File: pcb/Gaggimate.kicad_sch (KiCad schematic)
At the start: 69 parts, among them J1 USB_C_Receptacle, J2 Conn_01x02, J3 Conn_01x03, J4 Conn_01x04, J5 Conn_01x04, J6 Conn_01x10, J7 Conn_01x02, J8 Conn_01x02, K1 Relay_SPDT, K2 Relay_SPDT, K3 Relay_SPDT, Q1 MMBT2222, Q2 MMBT2222, Q3 MMBT2222, SW1 SW_Push, SW2 SW_Push, U1 ESP32-S3-WROOM-1, U2 AMS1117-3.3, U6 MAX31855EASA

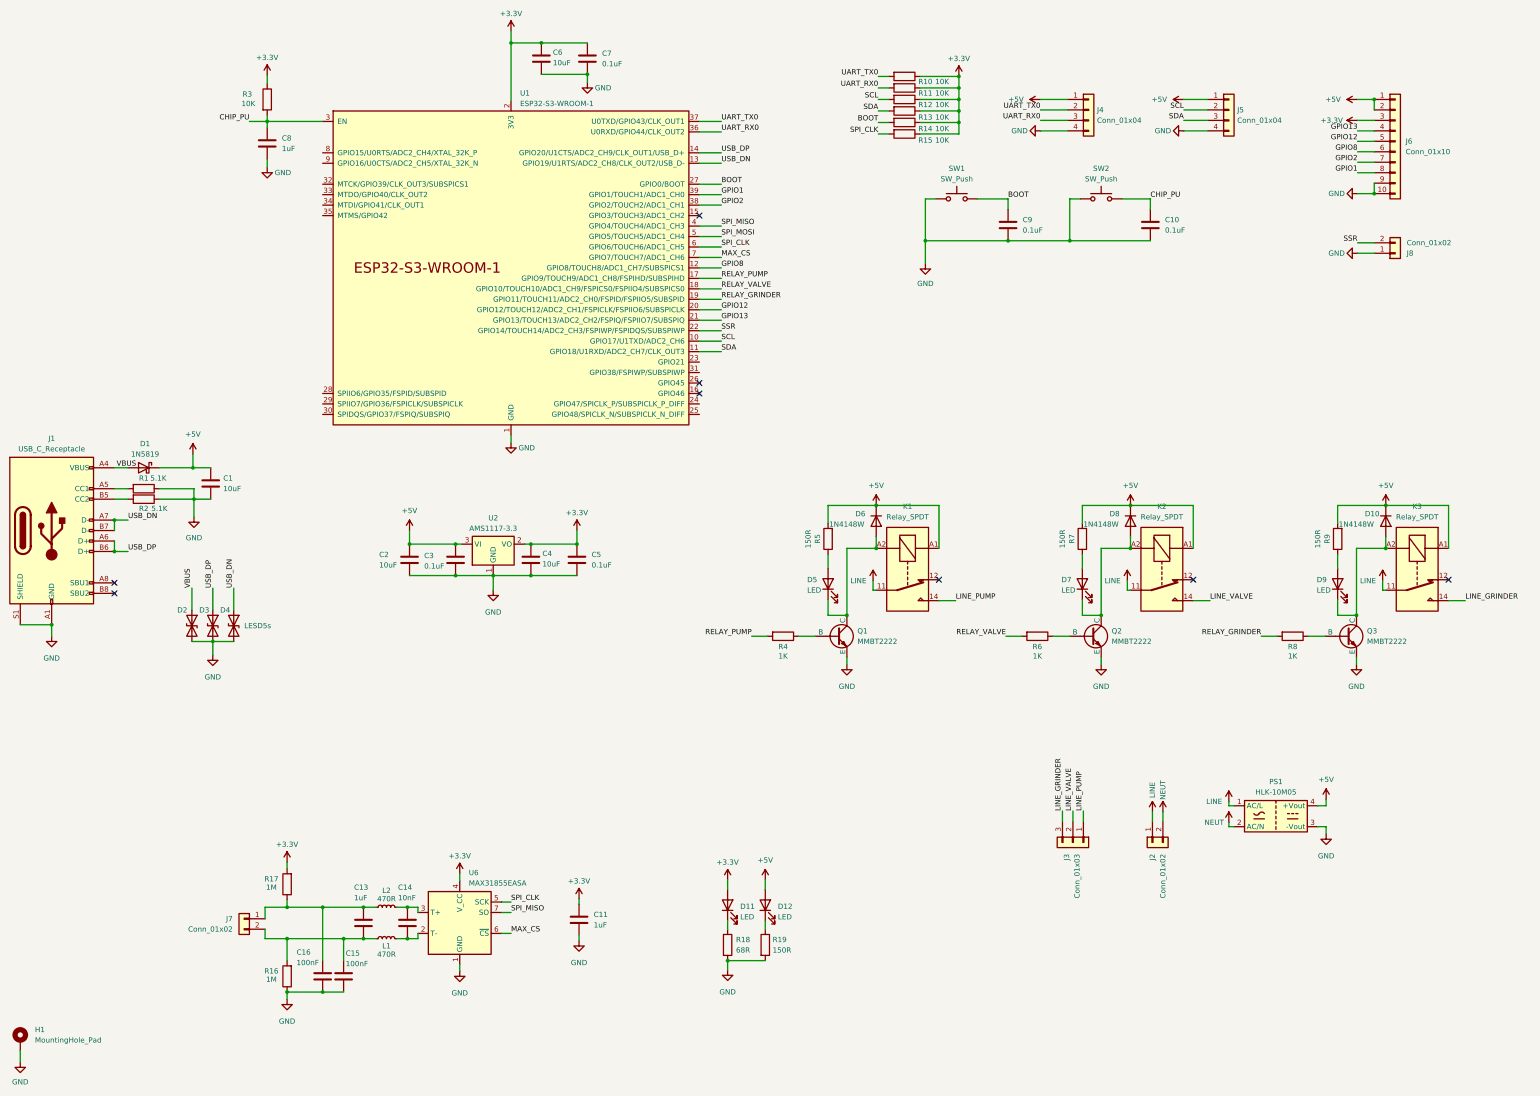
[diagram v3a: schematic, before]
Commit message: feat: Add button connector to PCB, change pcbdraw
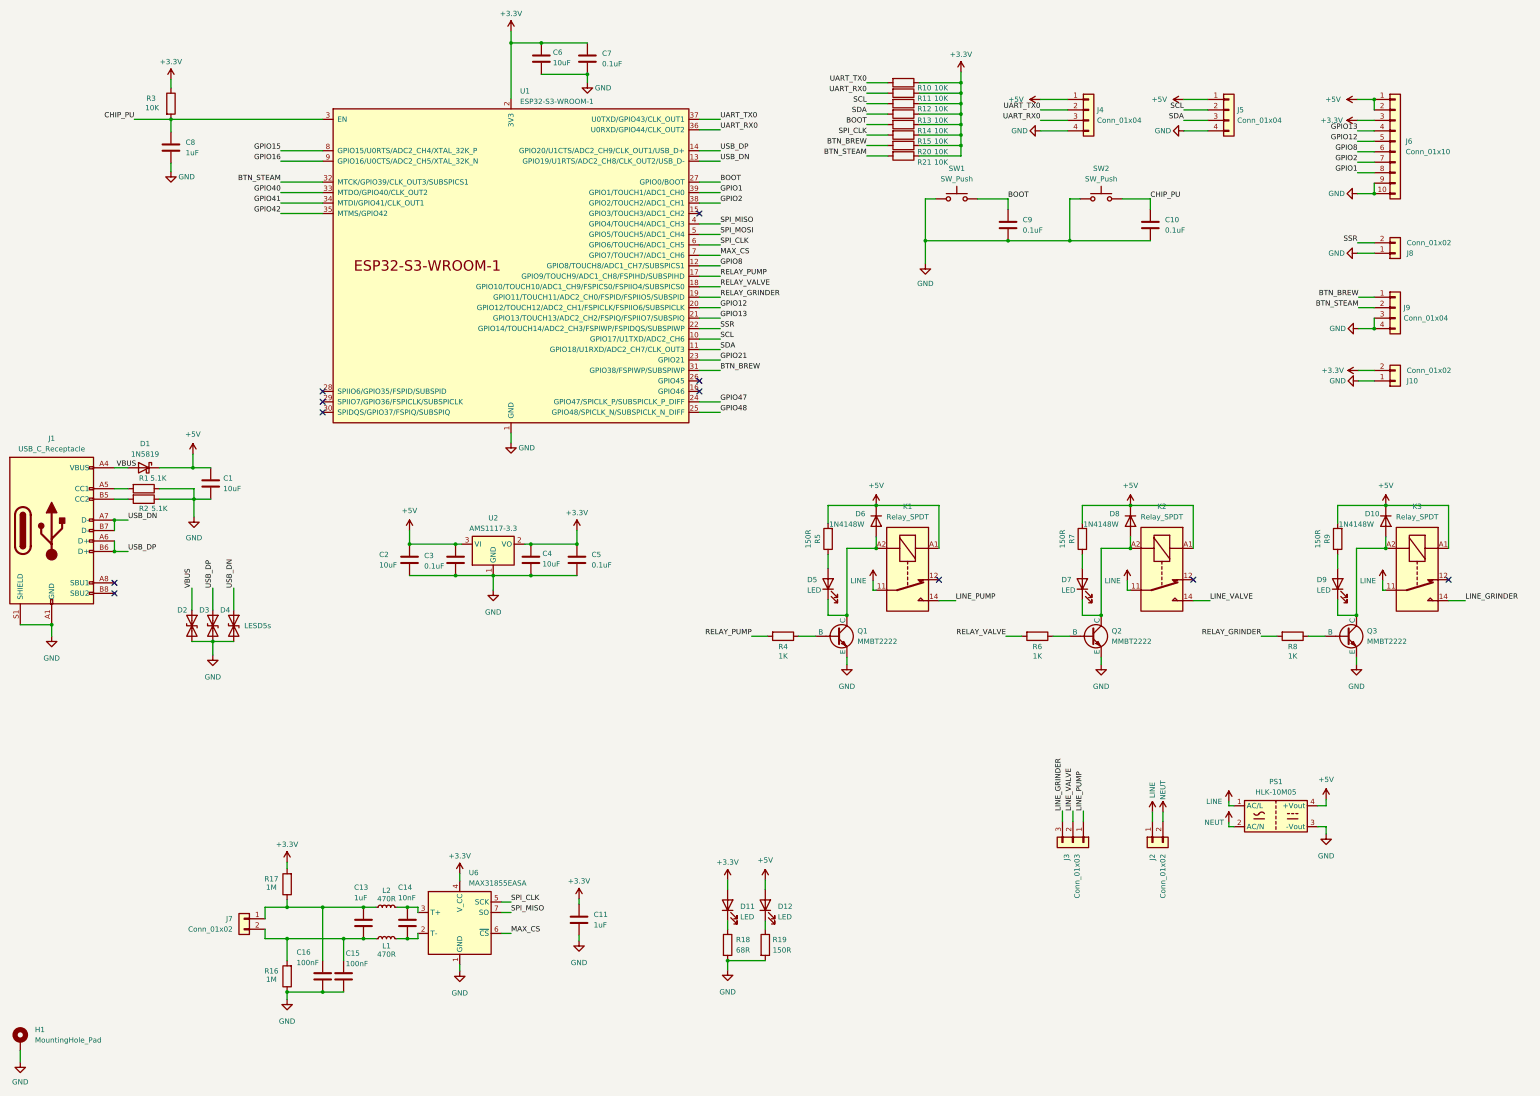
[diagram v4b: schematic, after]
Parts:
- added J10: Conn_01x02, Connector_JST:JST_XH_B2B-XH-A_1x02_P2.50mm_Vertical, symbol Connector_Generic:Conn_01x02
- added J9: Conn_01x04, Connector_JST:JST_XH_B4B-XH-A_1x04_P2.50mm_Vertical, symbol Connector_Generic:Conn_01x04
- added R20, R21: 10K, Resistor_SMD:R_0805_2012Metric, symbol Device:R
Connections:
- net +3.3V: now also J10.2 (Pin_2), R20.1, R21.1
- net GND: now also J10.1 (Pin_1), J9.3 (Pin_3), J9.4 (Pin_4)
- net GPIO21: now reaches U1.23 (GPIO21)
- net GPIO47: now reaches U1.24 (GPIO47/SPICLK_P/SUBSPICLK_P_DIFF)
- net GPIO48: now reaches U1.25 (GPIO48/SPICLK_N/SUBSPICLK_N_DIFF)
- net BTN_BREW: now reaches U1.31 (GPIO38/FSPIWP/SUBSPIWP)
- net BTN_BREW: now also J9.1 (Pin_1), R20.2
- net BTN_STEAM: now reaches U1.32 (MTCK/GPIO39/CLK_OUT3/SUBSPICS1)
- net BTN_STEAM: now also J9.2 (Pin_2), R21.2
- net GPIO40: now reaches U1.33 (MTDO/GPIO40/CLK_OUT2)
- net GPIO41: now reaches U1.34 (MTDI/GPIO41/CLK_OUT1)
- net GPIO42: now reaches U1.35 (MTMS/GPIO42)
- net GPIO15: now reaches U1.8 (GPIO15/U0RTS/ADC2_CH4/XTAL_32K_P)
- net GPIO16: now reaches U1.9 (GPIO16/U0CTS/ADC2_CH5/XTAL_32K_N)
- no-connect marks 8 -> 11
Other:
- moved on the sheet: C8, R10, R11, R12, R13, R14, R3, U1

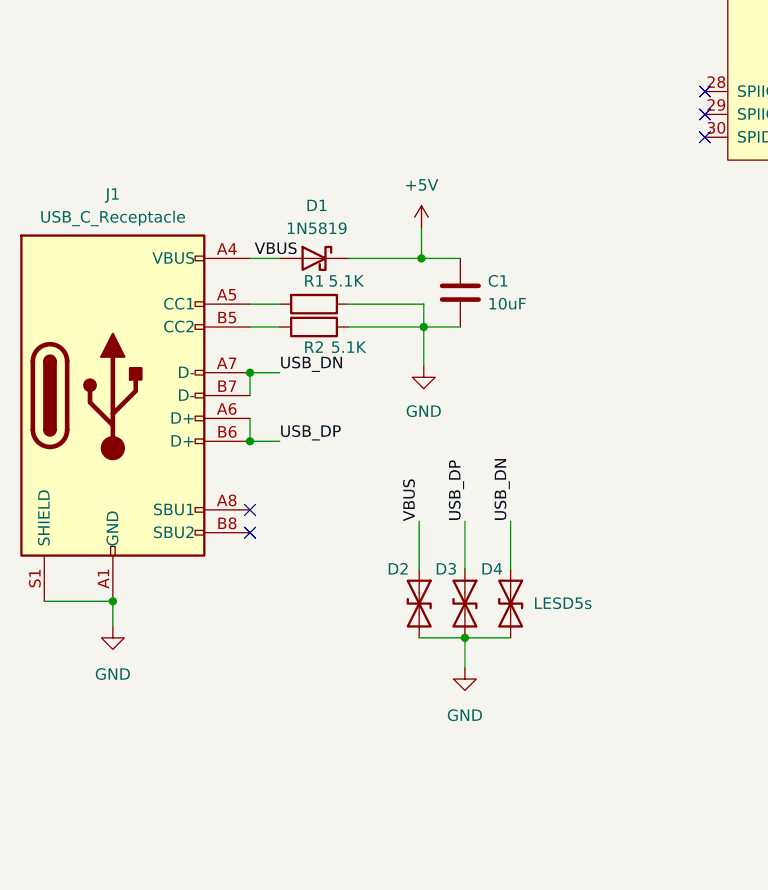
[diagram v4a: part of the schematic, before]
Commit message: feat: Replace diodes with usb protection chip
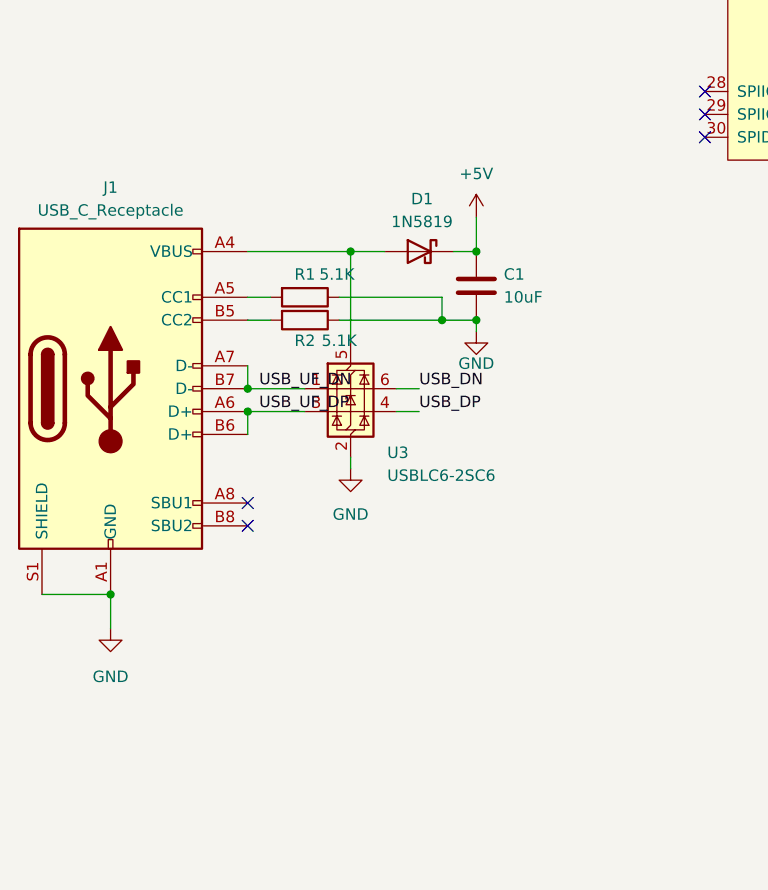
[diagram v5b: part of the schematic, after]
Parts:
- removed D2, D3, D4: LESD5s, Diode_SMD:D_SOD-523, symbol Device:D_TVS
- added U3: USBLC6-2SC6, Package_TO_SOT_SMD:SOT-23-6, symbol Power_Protection:USBLC6-2SC6
- J4, J5: LCSC (none) -> C144395
- J6: LCSC (none) -> C5383117
- J8: LCSC (none) -> C158012
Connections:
- net GND: now also U3.2 (GND)
- net USB_DN: now also U3.6 (I/O1); no longer J1.A7 (D-), J1.B7 (D-)
- net USB_DP: now also U3.4 (I/O2); no longer J1.A6 (D+), J1.B6 (D+)
- net VBUS: no longer names the net of D1.2 (A), J1.A4 (VBUS), J1.A9 (VBUS), J1.B4 (VBUS), J1.B9 (VBUS)
- net VBUS: now also U3.5 (VBUS)
- new net USB_UF_DN: J1.A7 (D-), J1.B7 (D-), U3.1 (I/O1)
- new net USB_UF_DP: J1.A6 (D+), J1.B6 (D+), U3.3 (I/O2)
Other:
- moved on the sheet: C1, D1, J1, R1, R2

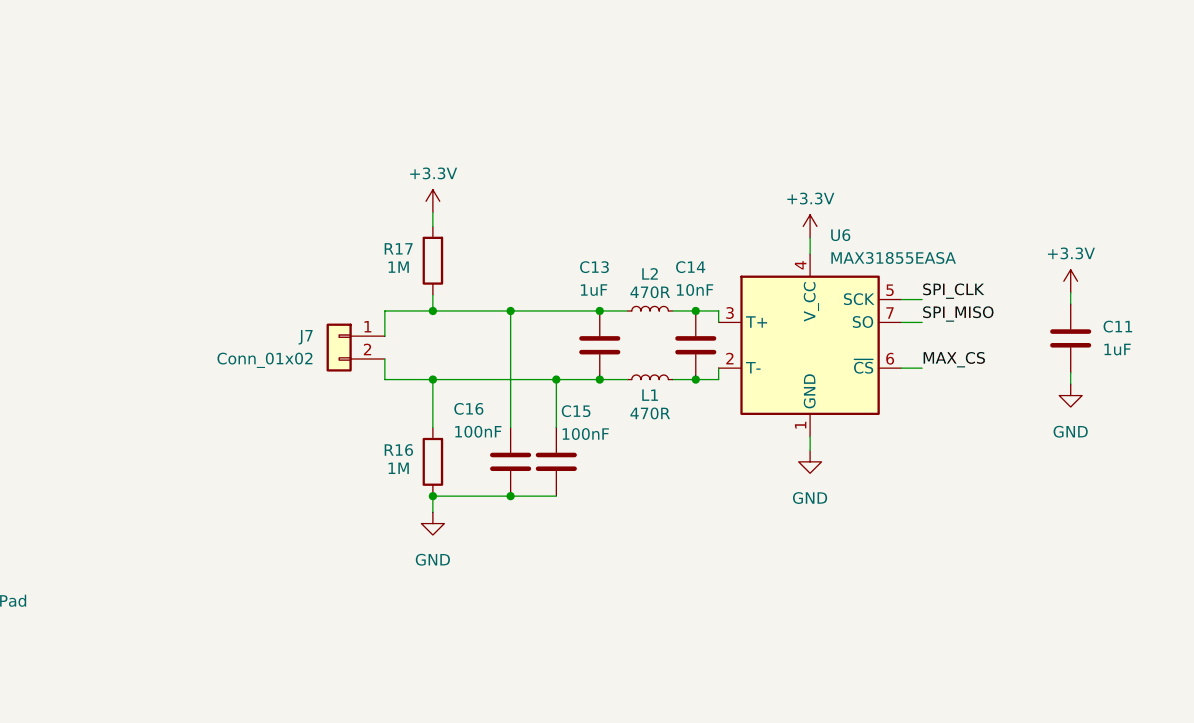
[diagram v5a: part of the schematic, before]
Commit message: feat: Simplify MAX31885 circuit, add silkscreen pinout
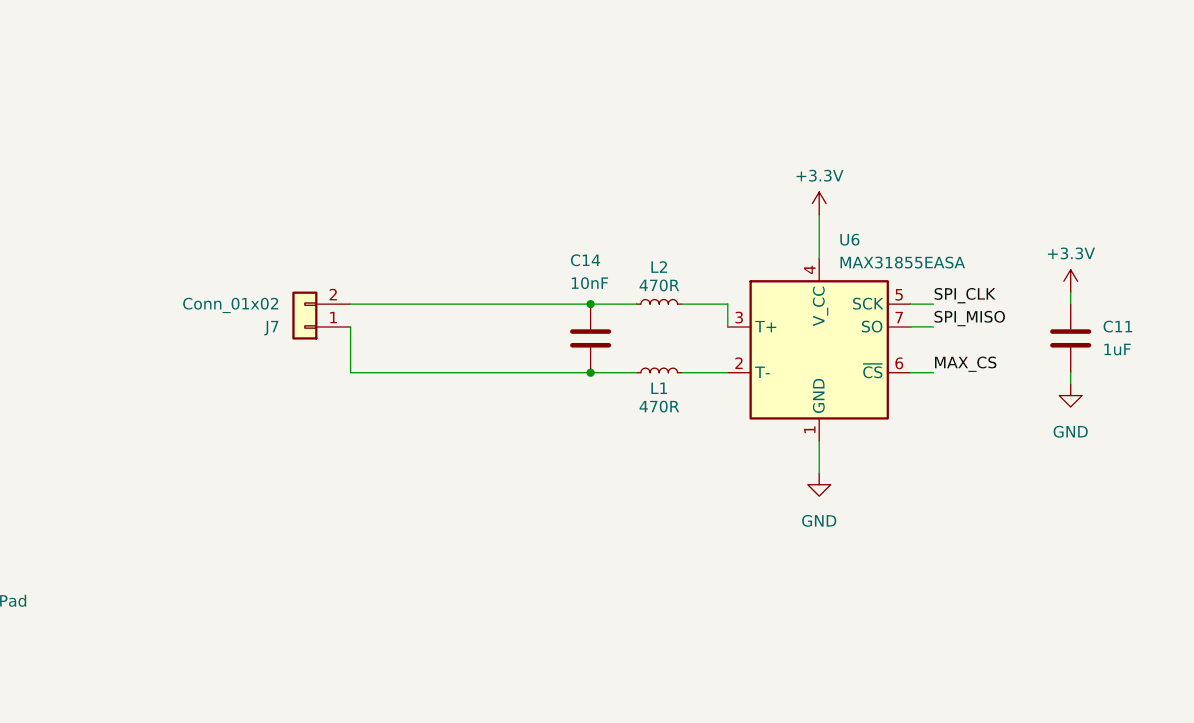
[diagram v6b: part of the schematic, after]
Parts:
- removed C13: 1uF, Capacitor_SMD:C_0805_2012Metric, symbol Device:C
- removed C15, C16: 100nF, Capacitor_SMD:C_0805_2012Metric, symbol Device:C
- removed R16, R17: 1M, Resistor_SMD:R_0805_2012Metric, symbol Device:R
- J10: LCSC (none) -> C158012
- J2: LCSC C2683165 -> C409161
- J3: LCSC C2683166 -> C409163
- J7: LCSC C5481312 -> C415432
- SW1, SW2: LCSC C221896 -> C2909692
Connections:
- net at L1.1: now also C14.2, J7.1 (Pin_1); no longer J7.2 (Pin_2)
- net at L1.2, U6.2 (T-): no longer C14.2
- net at L2.2, U6.3 (T+): no longer C14.1
- net at L2.1: now also C14.1, J7.2 (Pin_2); no longer J7.1 (Pin_1)
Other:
- moved on the sheet: C14, J7, L1, L2, U6

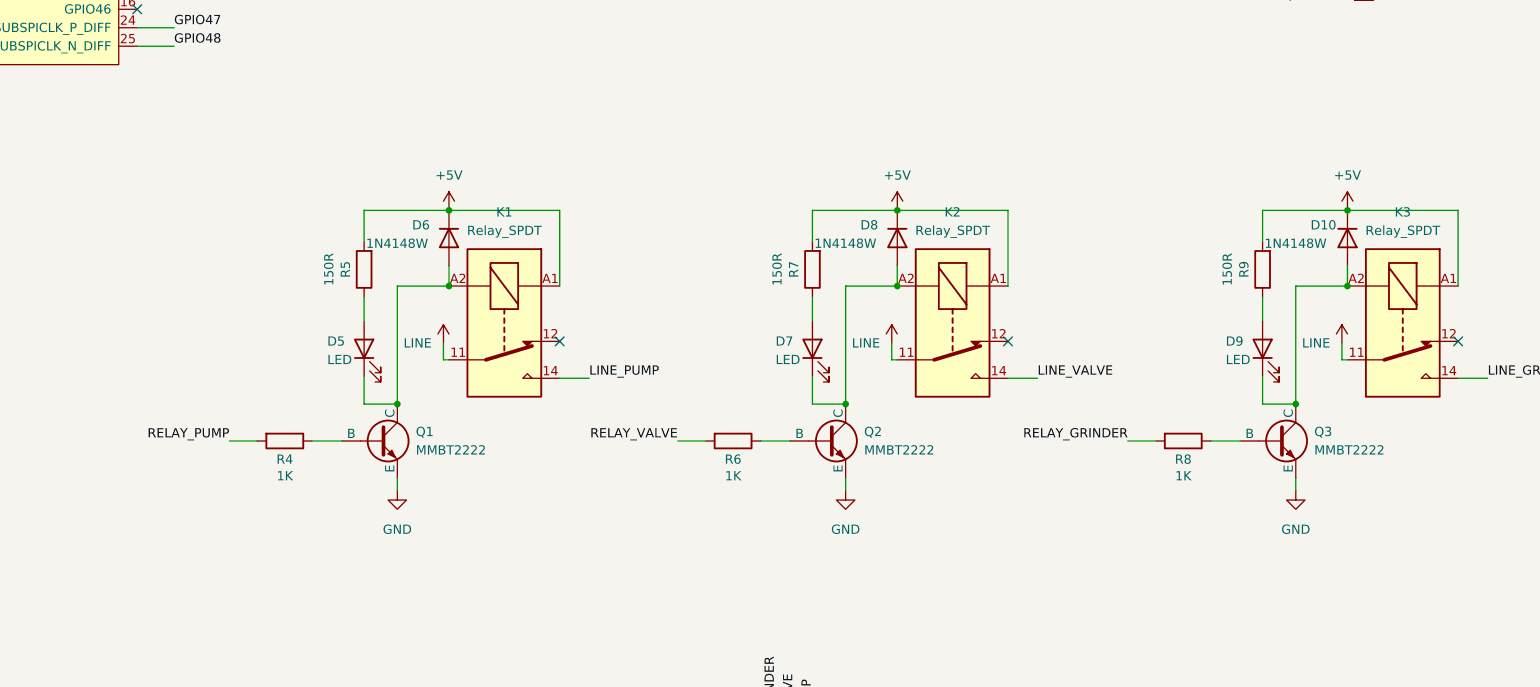
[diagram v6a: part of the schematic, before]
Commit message: feat: Fix PCB label, add render
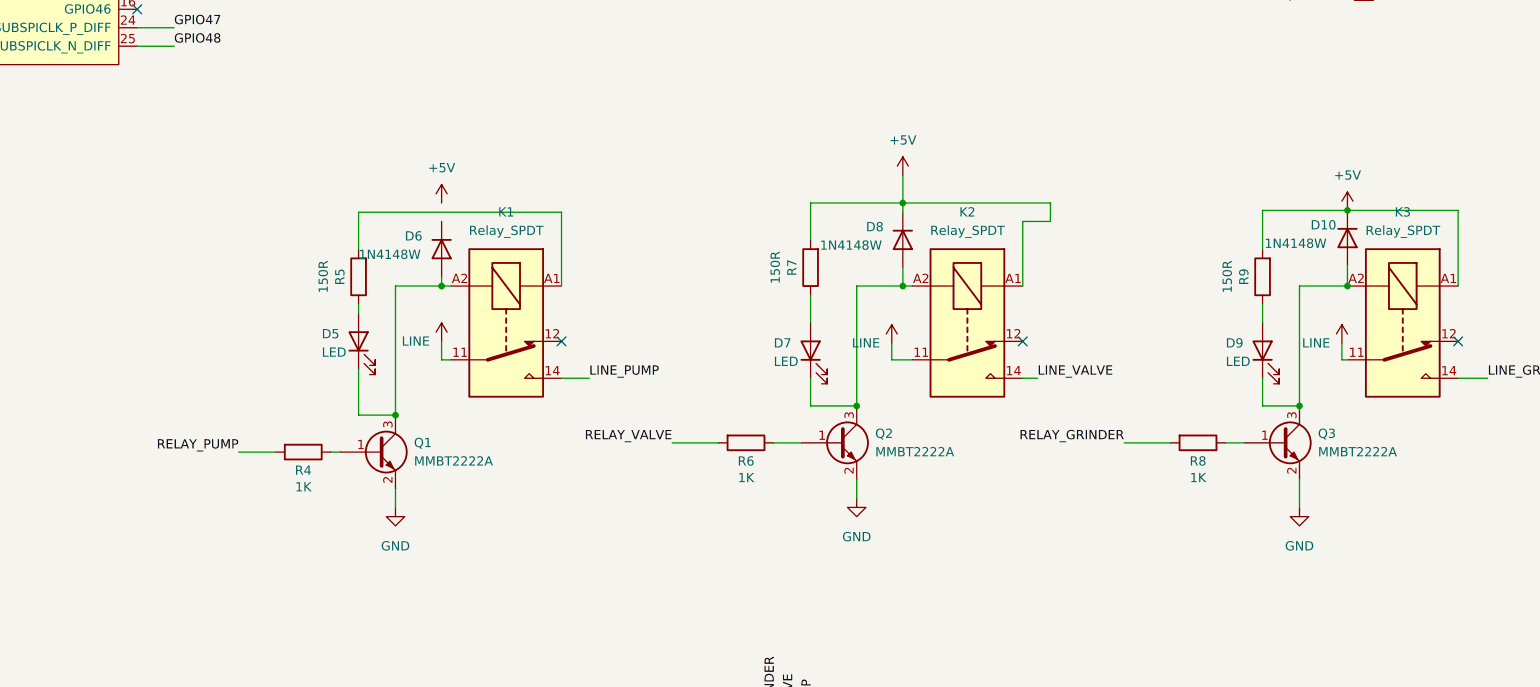
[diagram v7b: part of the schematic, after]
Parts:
- removed Q1, Q2, Q3: MMBT2222, Package_TO_SOT_SMD:SOT-23-3, symbol Simulation_SPICE:NPN
- added Q1, Q2, Q3: MMBT2222A, Package_TO_SOT_SMD:SOT-23, symbol Transistor_BJT:MMBT2222A
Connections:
- net +5V: no longer D6.1 (K), K1.A1, R5.2
- net GND: now also Q1.2 (E), Q2.2 (E), Q3.2 (E)
- net at D5.1 (K), D6.2 (A), K1.A2: now also Q1.3 (C)
- net at D10.2 (A), D9.1 (K), K3.A2: now also Q3.3 (C)
- net at R8.1: now also Q3.1 (B)
- net at D7.1 (K), D8.2 (A), K2.A2: now also Q2.3 (C)
- net at R4.1: now also Q1.1 (B)
- net at R6.1: now also Q2.1 (B)
- new net: K1.A1, R5.2
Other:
- moved on the sheet: D5, D6, D8, K2, R4, R5, R6, R8, R9

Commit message: feat: Add expansion mounting hole to PCB, add expansion template
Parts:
- Q1, Q2, Q3: LCSC (none) -> C916372
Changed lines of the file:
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@@
 			)
 		)
+		(property "LCSC" "C916372"
+			(at 236.22 167.6399 0)
+			(effects
+				(font
+					(size 1.27 1.27)
+				)
+				(hide yes)
+			)
+		)
 		(pin "2"
 		)
@@
 			)
 		)
+		(property "LCSC" "C916372"
+			(at 360.68 166.3699 0)
+			(effects
+				(font
+					(size 1.27 1.27)
+				)
+				(hide yes)
+			)
+		)
 		(pin "2"
 		)
@@
 			(effects
 				(font
+					(size 1.27 1.27)
+				)
+				(hide yes)
+			)
+		)
+		(property "LCSC" "C916372"
+			(at 299.72 166.3699 0)
+			(effects
+				(font
